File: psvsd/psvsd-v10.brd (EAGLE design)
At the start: 30 x 33.4 mm, 30 parts, among them J1 TRANSFLASH-PUSH, U1 USB2244QFN, U3 VREG, Y1 24.000MHz

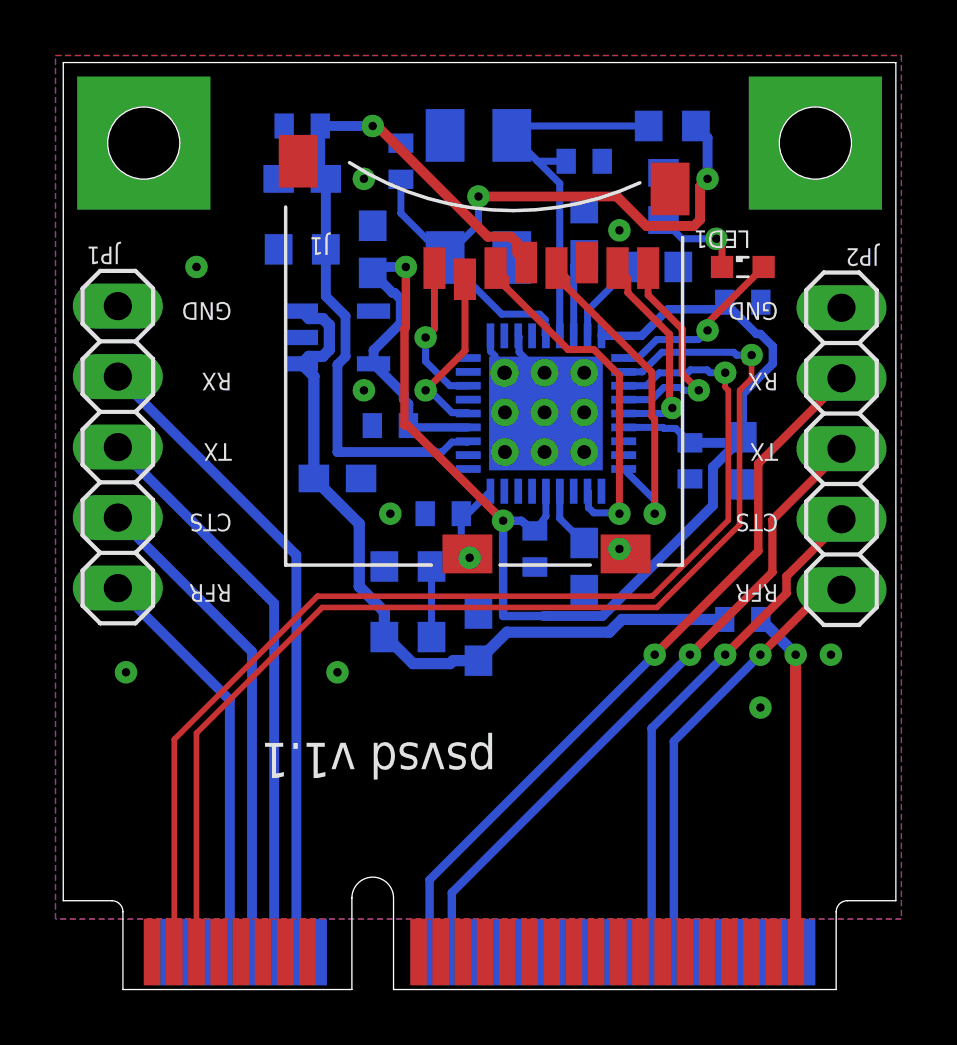
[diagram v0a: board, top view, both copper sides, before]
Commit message: Moved two GND pin routing out of the flag since it is discouraged
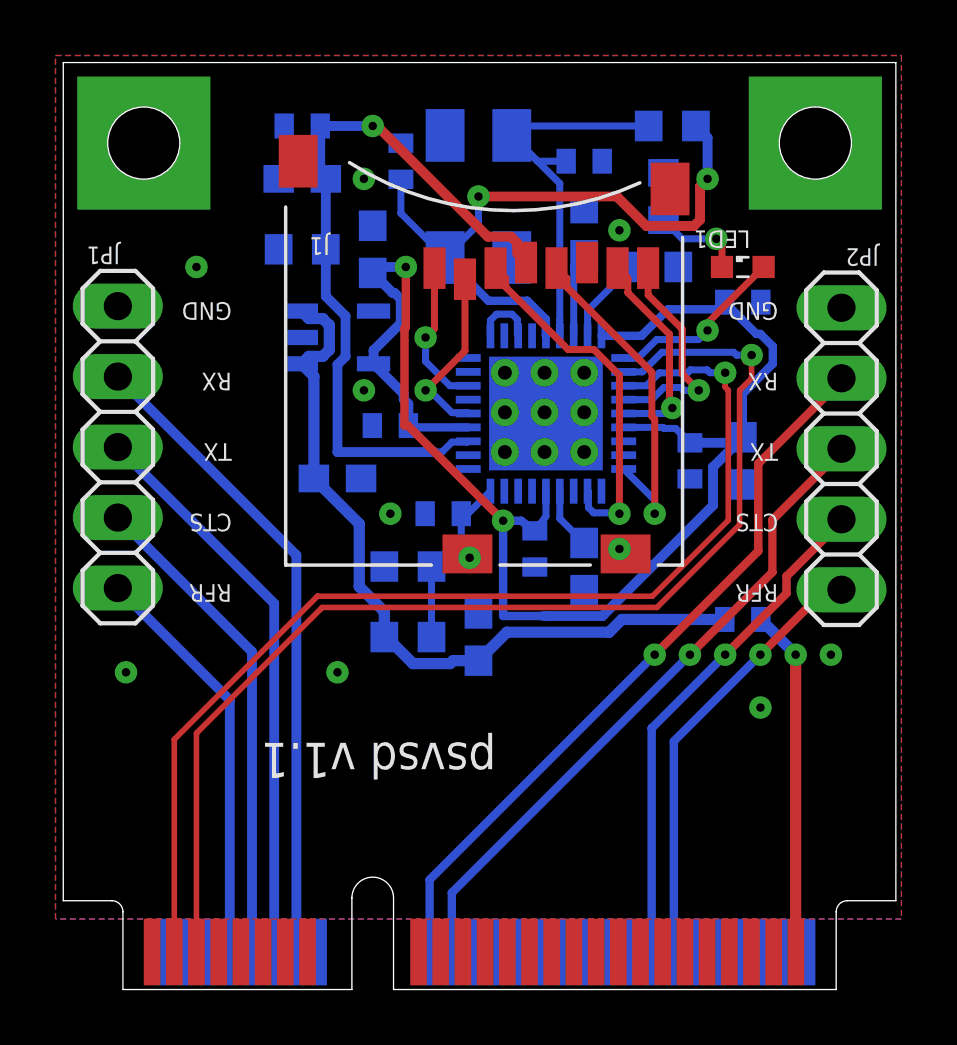
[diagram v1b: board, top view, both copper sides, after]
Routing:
- net GND: track 3.20 -> 2.54 mm, vias 21 -> 20
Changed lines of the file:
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@@
 <grid distance="0.025" unitdist="inch" unit="inch" style="lines" multiple="1" display="yes" altdistance="0.0125" altunitdist="inch" altunit="inch"/>
 <layers>
-<layer number="1" name="Top" color="4" fill="1" visible="no" active="yes"/>
-<layer number="16" name="Bottom" color="1" fill="1" visible="no" active="yes"/>
+<layer number="1" name="Top" color="4" fill="1" visible="yes" active="yes"/>
+<layer number="16" name="Bottom" color="1" fill="1" visible="yes" active="yes"/>
 <layer number="17" name="Pads" color="2" fill="1" visible="yes" active="yes"/>
 <layer number="18" name="Vias" color="2" fill="1" visible="yes" active="yes"/>
@@
 <layer number="20" name="Dimension" color="15" fill="1" visible="yes" active="yes"/>
 <layer number="21" name="tPlace" color="7" fill="1" visible="no" active="yes"/>
-<layer number="22" name="bPlace" color="7" fill="1" visible="yes" active="yes"/>
+<layer number="22" name="bPlace" color="7" fill="1" visible="no" active="yes"/>
 <layer number="23" name="tOrigins" color="15" fill="1" visible="no" active="yes"/>
-<layer number="24" name="bOrigins" color="15" fill="1" visible="yes" active="yes"/>
+<layer number="24" name="bOrigins" color="15" fill="1" visible="no" active="yes"/>
 <layer number="25" name="tNames" color="7" fill="1" visible="no" active="yes"/>
-<layer number="26" name="bNames" color="7" fill="1" visible="yes" active="yes"/>
+<layer number="26" name="bNames" color="7" fill="1" visible="no" active="yes"/>
 <layer number="27" name="tValues" color="7" fill="1" visible="no" active="yes"/>
-<layer number="28" name="bValues" color="7" fill="1" visible="yes" active="yes"/>
+<layer number="28" name="bValues" color="7" fill="1" visible="no" active="yes"/>
 <layer number="29" name="tStop" color="7" fill="3" visible="no" active="yes"/>
 <layer number="30" name="bStop" color="7" fill="6" visible="no" active="yes"/>
@@
 <contactref element="C4" pad="1"/>
 <contactref element="C3" pad="2"/>
-<via x="17.4371" y="24.13" extent="1-16" drill="0.5"/>
 <via x="18.89125" y="24.13" extent="1-16" drill="0.5"/>
 <via x="20.32" y="24.13" extent="1-16" drill="0.5"/>
@@
 <via x="12.3825" y="23.495" extent="1-16" drill="0.3048"/>
 <via x="13.335" y="19.05" extent="1-16" drill="0.3048"/>
-<wire x1="16.942" y1="25.46" x2="16.942" y2="24.903025" width="0.254" layer="16"/>
-<wire x1="16.942" y1="24.903025" x2="17.1125125" y2="24.7325125" width="0.254" layer="16"/>
-<wire x1="17.942" y1="25.46" x2="17.9718" y2="25.4302" width="0.254" layer="16"/>
-<wire x1="17.9718" y1="25.4302" x2="17.9718" y2="24.873225" width="0.254" layer="16"/>
-<wire x1="18.415" y1="24.430025" x2="18.415" y2="23.495" width="0.254" layer="16"/>
-<wire x1="17.9718" y1="24.873225" x2="18.415" y2="24.430025" width="0.254" layer="16"/>
 <via x="12.3825" y="31.115" extent="1-16" drill="0.3048"/>
 <via x="21.59" y="29.2608" extent="1-16" drill="0.3048"/>
@@
 <contactref element="R6" pad="2"/>
 <via x="29.21" y="13.97" extent="1-16" drill="0.3048"/>
+<wire x1="16.942" y1="25.46" x2="16.942" y2="26.016975" width="0.254" layer="16"/>
+<wire x1="17.165225" y1="26.2402" x2="17.718775" y2="26.2402" width="0.254" layer="16"/>
+<wire x1="17.718775" y1="26.2402" x2="17.9122" y2="26.046775" width="0.254" layer="16"/>
+<wire x1="17.9122" y1="26.046775" x2="17.9122" y2="25.4898" width="0.254" layer="16"/>
+<wire x1="17.9122" y1="25.4898" x2="17.942" y2="25.46" width="0.254" layer="16"/>
+<wire x1="16.942" y1="26.016975" x2="17.165225" y2="26.2402" width="0.254" layer="16"/>
 <wire x1="23.414" y1="30.75" x2="28.65" y2="32.405" width="0" layer="19" extent="1-1"/>
 <wire x1="23.1775" y1="31.33" x2="23.414" y2="30.75" width="0" layer="19" extent="1-16"/>
@@
 <wire x1="26.685" y1="26.67" x2="23.71" y2="27.94" width="0" layer="19" extent="16-16"/>
 <wire x1="29.591" y1="26.47" x2="26.685" y2="26.67" width="0" layer="19" extent="16-16"/>
-<wire x1="17.942" y1="25.46" x2="20.424" y2="28.1" width="0" layer="19" extent="1-16"/>
-<wire x1="18.89125" y1="24.13" x2="18.415" y2="24.430025" width="0" layer="19" extent="16-16"/>
-<wire x1="17.1125125" y1="24.7325125" x2="17.9718" y2="24.873225" width="0" layer="19" extent="16-16"/>
-<wire x1="17.4371" y1="24.13" x2="17.1125125" y2="24.7325125" width="0" layer="19" extent="16-16"/>
-<wire x1="17.4625" y1="24.13" x2="17.4371" y2="24.13" width="0" layer="19" extent="1-1"/>
-<wire x1="18.89125" y1="22.70125" x2="18.415" y2="23.495" width="0" layer="19" extent="16-16"/>
-<wire x1="18.942" y1="22.66" x2="18.89125" y2="22.70125" width="0" layer="19" extent="16-16"/>
-<wire x1="17.4625" y1="22.70125" x2="18.415" y2="23.495" width="0" layer="19" extent="16-16"/>
-<wire x1="20.32" y1="22.70125" x2="18.942" y2="22.66" width="0" layer="19" extent="16-16"/>
+<wire x1="17.9122" y1="26.046775" x2="20.424" y2="28.1" width="0" layer="19" extent="1-16"/>
+<wire x1="17.4625" y1="24.13" x2="17.942" y2="25.46" width="0" layer="19" extent="16-16"/>
+<wire x1="18.89125" y1="24.13" x2="17.4625" y2="24.13" width="0" layer="19" extent="1-1"/>
+<wire x1="20.32" y1="24.13" x2="18.89125" y2="24.13" width="0" layer="19" extent="1-1"/>
+<wire x1="20.32" y1="22.70125" x2="20.32" y2="24.13" width="0" layer="19" extent="1-1"/>
+<wire x1="18.942" y1="22.66" x2="20.32" y2="22.70125" width="0" layer="19" extent="16-16"/>
+<wire x1="18.89125" y1="22.70125" x2="18.942" y2="22.66" width="0" layer="19" extent="16-16"/>
 <wire x1="18.89125" y1="21.2725" x2="18.942" y2="22.66" width="0" layer="19" extent="16-16"/>
-<wire x1="20.32" y1="24.13" x2="18.89125" y2="24.13" width="0" layer="19" extent="1-1"/>
 <wire x1="20.32" y1="21.2725" x2="20.32" y2="22.70125" width="0" layer="19" extent="1-1"/>
-<wire x1="17.4625" y1="21.2725" x2="17.4625" y2="22.70125" width="0" layer="19" extent="1-1"/>
+<wire x1="17.4625" y1="22.70125" x2="17.4625" y2="24.13" width="0" layer="19" extent="1-1"/>
+<wire x1="17.4625" y1="21.2725" x2="18.89125" y2="21.2725" width="0" layer="19" extent="1-1"/>
 <wire x1="14.59" y1="19.05" x2="17.4625" y2="21.2725" width="0" layer="19" extent="16-16"/>
 <wire x1="13.335" y1="19.05" x2="14.59" y2="19.05" width="0" layer="19" extent="16-16"/>
@@
 <contactref element="R1" pad="2"/>
 <contactref element="U1" pad="33"/>
-<wire x1="19.442" y1="30.948" x2="19.442" y2="25.46" width="0.254" layer="16"/>
+<wire x1="19.442" y1="30.948" x2="19.442" y2="26.035" width="0.254" layer="16"/>
+<wire x1="19.442" y1="26.035" x2="19.442" y2="25.46" width="0.254" layer="16"/>
 <wire x1="17.71" y1="32.68" x2="19.442" y2="30.948" width="0.254" layer="16"/>
 <wire x1="19.67" y1="31.75" x2="18.64" y2="31.75" width="0.254" layer="16"/>
@@
 <contactref element="R1" pad="1"/>
 <contactref element="U1" pad="32"/>
-<wire x1="18.718775" y1="26.2402" x2="18.9122" y2="26.046775" width="0.254" layer="16"/>
-<wire x1="17.3498" y1="26.2402" x2="15.31" y2="28.28" width="0.254" layer="16"/>
-<wire x1="18.718775" y1="26.2402" x2="17.3498" y2="26.2402" width="0.254" layer="16"/>
-<wire x1="18.9122" y1="25.4898" x2="18.942" y2="25.46" width="0.254" layer="16"/>
-<wire x1="18.9122" y1="25.4898" x2="18.9122" y2="26.046775" width="0.254" layer="16"/>
 <via x="16.51" y="30.48" extent="1-16" drill="0.3048"/>
 <wire x1="16.51" y1="30.48" x2="16.51" y2="29.48" width="0.254" layer="16"/>
-<wire x1="16.51" y1="29.48" x2="15.31" y2="28.28" width="0.254" layer="16"/>
+<wire x1="15.31" y1="28.28" x2="16.51" y2="29.48" width="0.254" layer="16"/>
 <via x="24.765" y="31.115" extent="1-16" drill="0.3048"/>
 <wire x1="22.5561875" y1="29.419" x2="24.2718125" y2="29.419" width="0.3556" layer="1"/>
@@
 <wire x1="15.31" y1="28.28" x2="13.716" y2="29.874" width="0.254" layer="16"/>
 <wire x1="13.716" y1="29.874" x2="13.716" y2="31.1" width="0.254" layer="16"/>
+<wire x1="18.942" y1="25.46" x2="18.9376" y2="25.4644" width="0.3048" layer="16"/>
+<wire x1="18.9376" y1="25.4644" x2="18.9376" y2="26.05729375" width="0.3048" layer="16"/>
+<wire x1="16.8672" y1="26.7228" x2="15.31" y2="28.28" width="0.3048" layer="16"/>
+<wire x1="18.9376" y1="26.05729375" x2="18.27209375" y2="26.7228" width="0.3048" layer="16"/>
+<wire x1="18.27209375" y1="26.7228" x2="16.8672" y2="26.7228" width="0.3048" layer="16"/>
 </signal>
 <signal name="VDD5">

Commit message: Enhanced heat sink under chip
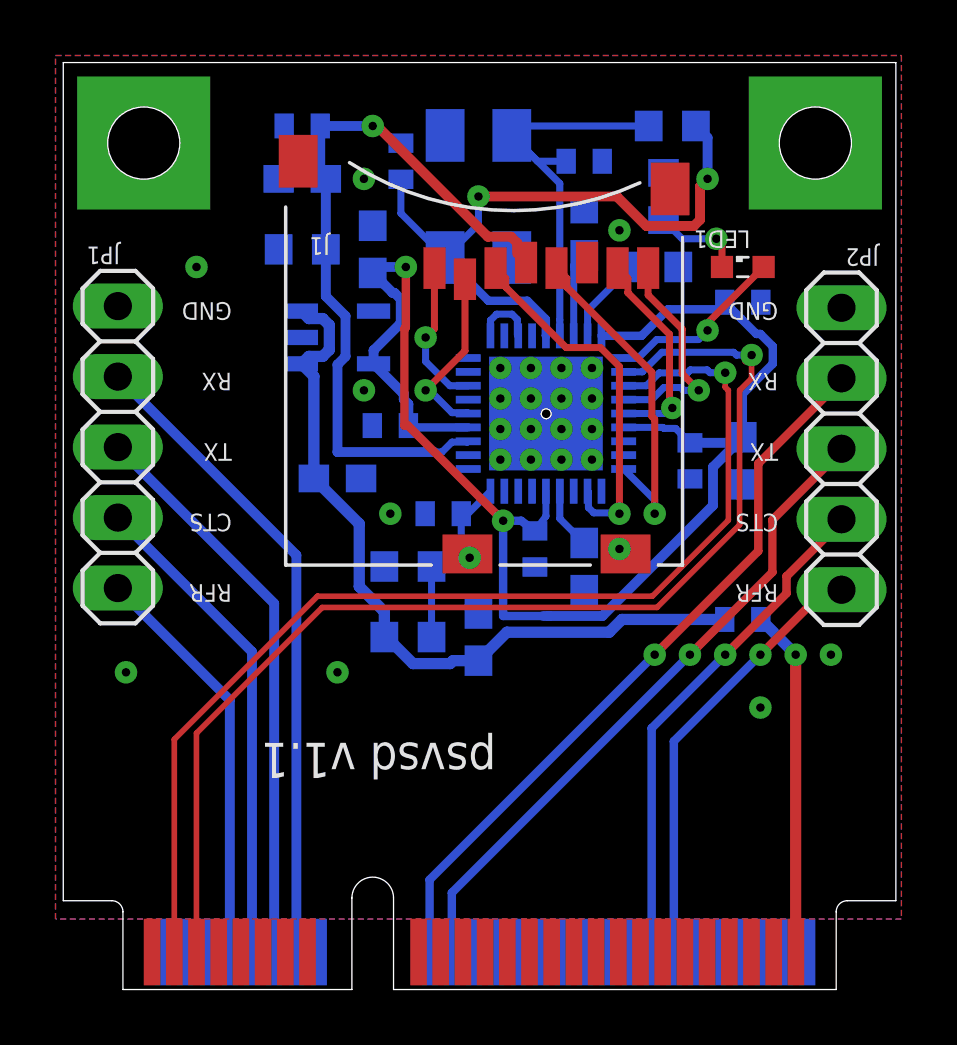
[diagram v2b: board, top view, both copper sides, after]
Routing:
- net GND: vias 20 -> 27

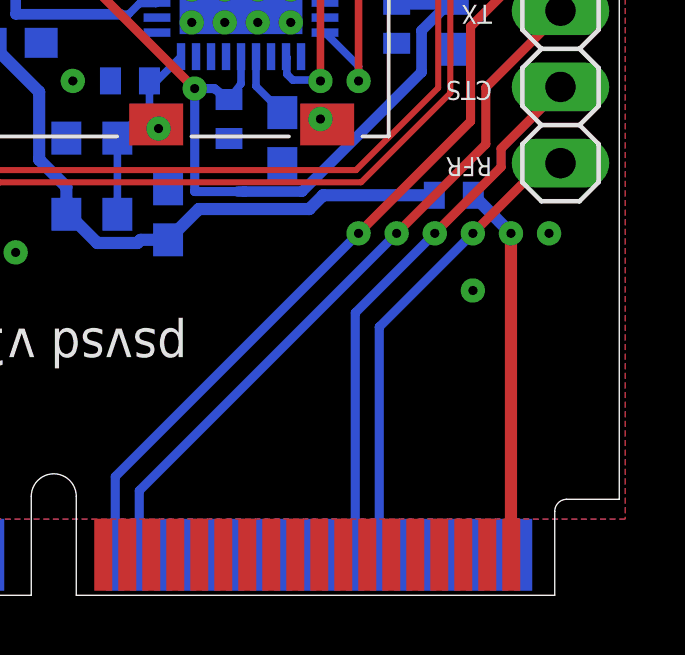
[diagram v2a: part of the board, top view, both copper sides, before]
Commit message: Added a power plane on top to dissipate the many +5V inputs
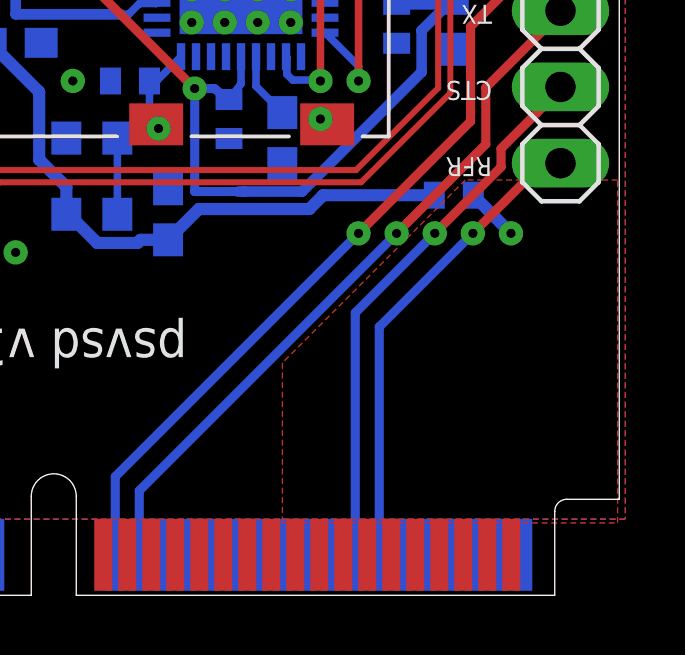
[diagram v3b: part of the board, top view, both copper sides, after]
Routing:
- net +5V: track 12.6 -> 1.86 mm
- net GND: vias 27 -> 25
- added copper zone on layer 1, net +5V
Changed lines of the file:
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@@
 <contactref element="C4" pad="1"/>
 <contactref element="C3" pad="2"/>
-<polygon width="0.254" layer="1">
+<polygon width="0.254" layer="1" rank="2">
 <vertex x="1.27" y="35.56"/>
 <vertex x="31.75" y="35.56"/>
@@
 <vertex x="1.27" y="4.445"/>
 </polygon>
-<polygon width="0.254" layer="16">
+<polygon width="0.254" layer="16" rank="2">
 <vertex x="1.27" y="35.56"/>
 <vertex x="31.75" y="35.56"/>
@@
 <wire x1="7.3198" y1="3.4248" x2="7.15" y2="3.255" width="0.254" layer="1"/>
 <via x="11.43" y="13.335" extent="1-16" drill="0.3048"/>
-<via x="26.67" y="12.065" extent="1-16" drill="0.3048"/>
 <via x="3.81" y="13.335" extent="1-16" drill="0.3048"/>
 <via x="6.35" y="27.94" extent="1-16" drill="0.3048"/>
 <via x="16.1925" y="17.4625" extent="1-16" drill="0.3048"/>
 <contactref element="R6" pad="2"/>
-<via x="29.21" y="13.97" extent="1-16" drill="0.3048"/>
 <wire x1="16.942" y1="25.46" x2="16.942" y2="26.016975" width="0.254" layer="16"/>
 <wire x1="17.165225" y1="26.2402" x2="17.718775" y2="26.2402" width="0.254" layer="16"/>
@@
 <via x="19.5" y="21" extent="1-16" drill="0.3048"/>
 <via x="20.6" y="21" extent="1-16" drill="0.3048"/>
+<wire x1="18.4" y1="23.2" x2="18.942" y2="22.66" width="0" layer="19" extent="16-16"/>
 <wire x1="21.59" y1="17.78" x2="21.814" y2="17.6" width="0" layer="19" extent="1-1"/>
 <wire x1="16.35" y1="3.255" x2="15.95" y2="3.255" width="0" layer="19" extent="1-16"/>
 <wire x1="23.1775" y1="31.33" x2="23.414" y2="30.75" width="0" layer="19" extent="1-16"/>
-<wire x1="18.942" y1="22.66" x2="18.4" y2="23.2" width="0" layer="19" extent="16-16"/>
 <wire x1="16.942" y1="25.46" x2="17.3" y2="24.3" width="0" layer="19" extent="16-16"/>
 </signal>
@@
 <wire x1="26.685" y1="15.24" x2="27.94" y2="13.97" width="0.4064" layer="16"/>
 <via x="27.94" y="13.97" extent="1-16" drill="0.3048"/>
-<wire x1="27.94" y1="13.97" x2="27.94" y2="3.265" width="0.4064" layer="1"/>
 <wire x1="27.94" y1="3.265" x2="27.95" y2="3.255" width="0.4064" layer="1"/>
-<wire x1="27.15" y1="3.255" x2="27.94" y2="3.265" width="0" layer="19" extent="1-1"/>
-<wire x1="26.35" y1="3.255" x2="27.15" y2="3.255" width="0" layer="19" extent="1-1"/>
-<wire x1="25.55" y1="3.255" x2="26.35" y2="3.255" width="0" layer="19" extent="1-1"/>
-<wire x1="24.75" y1="3.255" x2="25.55" y2="3.255" width="0" layer="19" extent="1-1"/>
-<wire x1="23.95" y1="3.255" x2="24.75" y2="3.255" width="0" layer="19" extent="1-1"/>
-<wire x1="23.15" y1="3.255" x2="23.95" y2="3.255" width="0" layer="19" extent="1-1"/>
-<wire x1="22.35" y1="3.255" x2="23.15" y2="3.255" width="0" layer="19" extent="1-1"/>
-<wire x1="21.59" y1="3.295" x2="22.35" y2="3.255" width="0" layer="19" extent="1-1"/>
-<wire x1="20.75" y1="3.255" x2="21.55" y2="3.255" width="0" layer="19" extent="1-1"/>
+<polygon width="0.254" layer="1">
+<vertex x="20.32" y="4.318"/>
+<vertex x="31.496" y="4.318"/>
+<vertex x="31.496" y="15.748"/>
+<vertex x="26.416" y="15.748"/>
+<vertex x="20.32" y="9.652"/>
+</polygon>
 </signal>
 <signal name="SD_D0">
